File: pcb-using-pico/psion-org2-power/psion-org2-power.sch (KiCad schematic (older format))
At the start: 52 parts, among them J1 Conn_02x08_Odd_Even, J2 Conn_02x08_Odd_Even, J3 Conn_01x27_Female, J4 Conn_02x08_Odd_Even, J5 Conn_01x11_Female, J6 Conn_01x02_Female, J7 Conn_01x03_Female, M1 P-CHANNEL-MOSFET, M2 P-CHANNEL-MOSFET, U1 ESP32-WROOM-32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

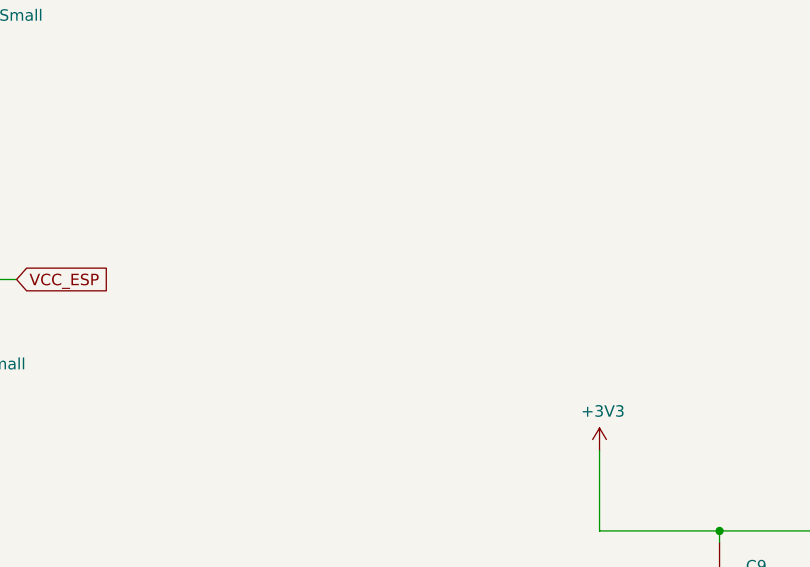
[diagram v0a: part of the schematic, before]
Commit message: V1.1 PCBs
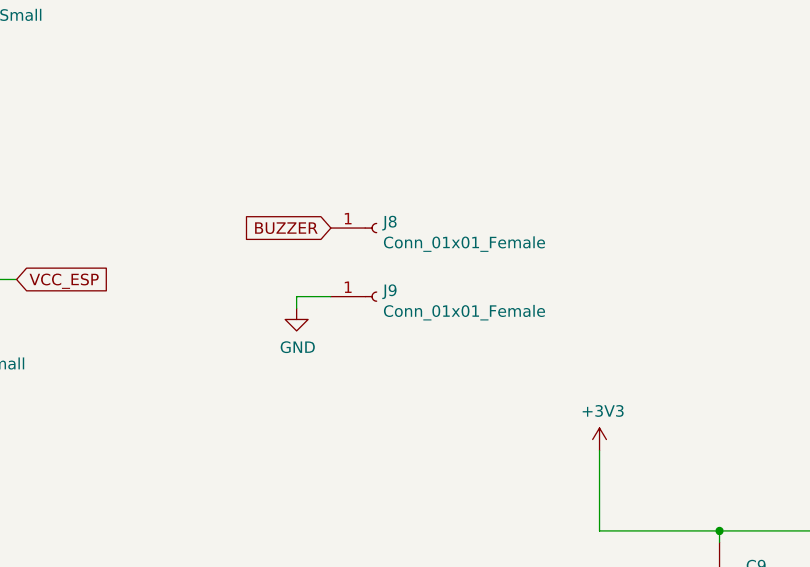
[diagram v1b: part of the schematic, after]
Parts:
- added J8, J9: Conn_01x01_Female, ajm_kicad:psion_beeper_pad, symbol Connector:Conn_01x01_Female
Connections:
- net BUZZER: now also J8.1 (Pin_1)
- net GND: now also J9.1 (Pin_1)
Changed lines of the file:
@@
 Wire Wire Line
 	14600 1800 14850 1800
+$Comp
+L Connector:Conn_01x01_Female J8
+U 1 1 622FDD65
+P 5600 6975
+F 0 "J8" H 5628 7001 50  0000 L CNN
+F 1 "Conn_01x01_Female" H 5628 6910 50  0000 L CNN
+F 2 "ajm_kicad:psion_beeper_pad" H 5600 6975 50  0001 C CNN
+F 3 "~" H 5600 6975 50  0001 C CNN
+	1    5600 6975
+	1    0    0    -1
+$EndComp
+$Comp
+L Connector:Conn_01x01_Female J9
+U 1 1 622FE035
+P 5600 7275
+F 0 "J9" H 5628 7301 50  0000 L CNN
+F 1 "Conn_01x01_Female" H 5628 7210 50  0000 L CNN
+F 2 "ajm_kicad:psion_beeper_pad" H 5600 7275 50  0001 C CNN
+F 3 "~" H 5600 7275 50  0001 C CNN
+	1    5600 7275
+	1    0    0    -1
+$EndComp
+$Comp
+L power:GND #PWR0132
+U 1 1 622FEC3B
+P 5250 7325
+F 0 "#PWR0132" H 5250 7075 50  0001 C CNN
+F 1 "GND" H 5255 7152 50  0000 C CNN
+F 2 "" H 5250 7325 50  0001 C CNN
+F 3 "" H 5250 7325 50  0001 C CNN
+	1    5250 7325
+	1    0    0    -1
+$EndComp
+Wire Wire Line
+	5250 7325 5250 7275
+Wire Wire Line
+	5250 7275 5400 7275
+Text GLabel 5400 6975 0    50   Input ~ 0
+BUZZER
 $EndSCHEMATC

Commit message: Updates
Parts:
- R1, R13, R14: value 100k -> 10k
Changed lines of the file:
@@
 P 2275 3125
 F 0 "R1" H 2334 3171 50  0000 L CNN
-F 1 "100k" H 2334 3080 50  0000 L CNN
+F 1 "10k" H 2334 3080 50  0000 L CNN
 F 2 "Resistor_SMD:R_0805_2012Metric" H 2275 3125 50  0001 C CNN
 F 3 "~" H 2275 3125 50  0001 C CNN
@@
 P 10075 6775
 F 0 "R13" H 10134 6821 50  0000 L CNN
-F 1 "100k" H 10134 6730 50  0000 L CNN
+F 1 "10k" H 10134 6730 50  0000 L CNN
 F 2 "Resistor_SMD:R_0805_2012Metric" H 10075 6775 50  0001 C CNN
 F 3 "~" H 10075 6775 50  0001 C CNN
@@
 P 10075 7500
 F 0 "R14" H 10134 7546 50  0000 L CNN
-F 1 "100k" H 10134 7455 50  0000 L CNN
+F 1 "10k" H 10134 7455 50  0000 L CNN
 F 2 "Resistor_SMD:R_0805_2012Metric" H 10075 7500 50  0001 C CNN
 F 3 "~" H 10075 7500 50  0001 C CNN

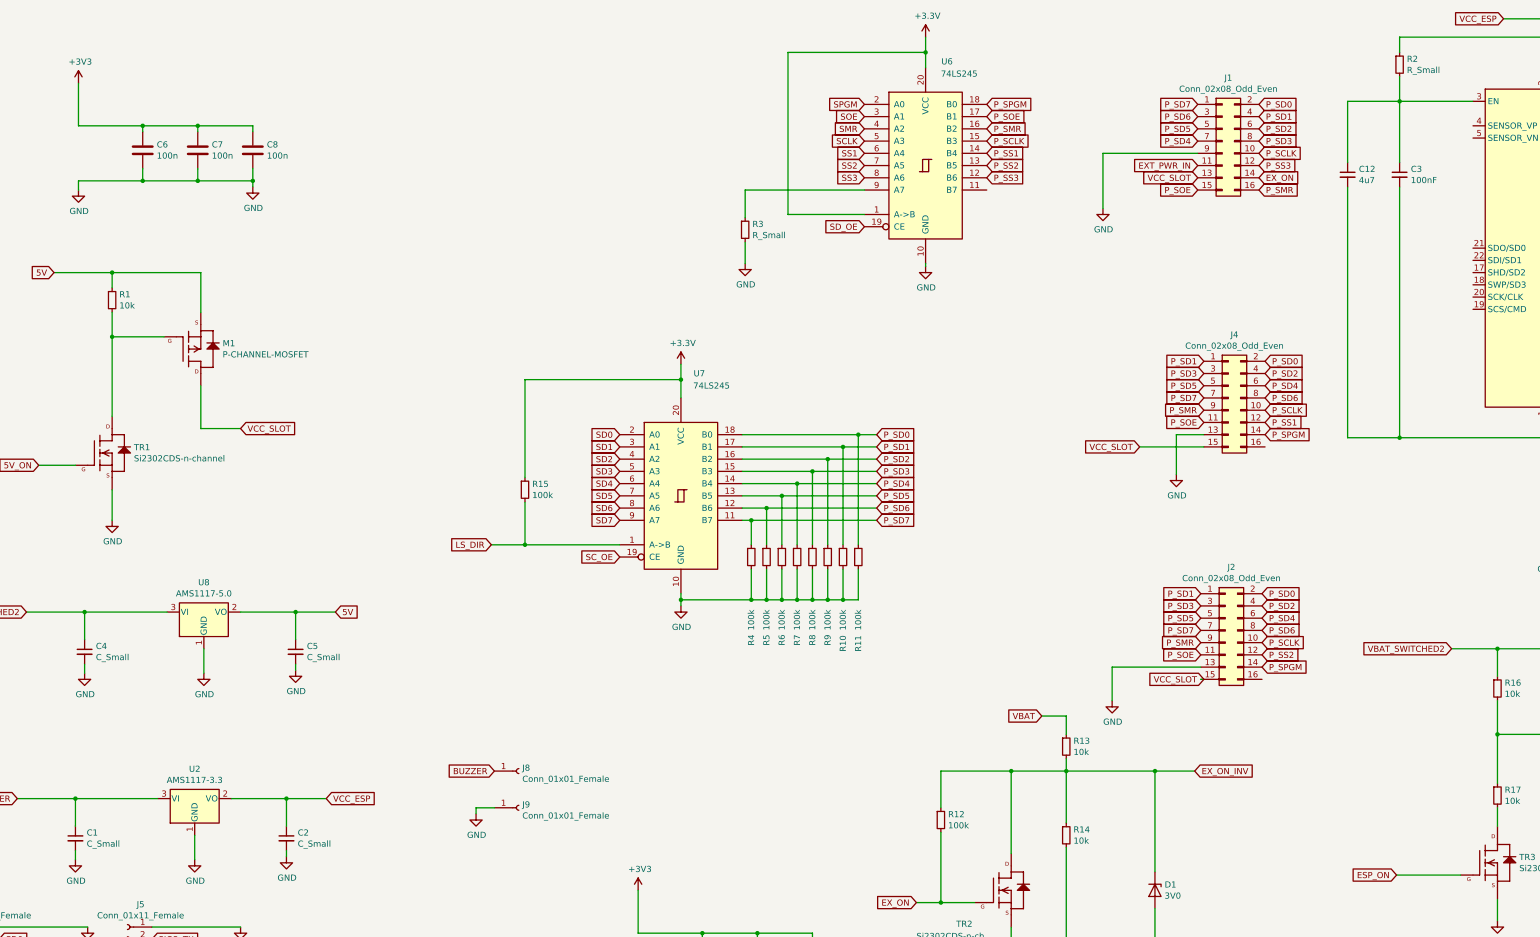
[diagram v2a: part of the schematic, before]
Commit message: Updated missing values on schematics, pushed those through to the PCB and created BOM .csv files for those schematics. Created .pdf files for schematics to mitigate the missing library problem of Kicad 5.
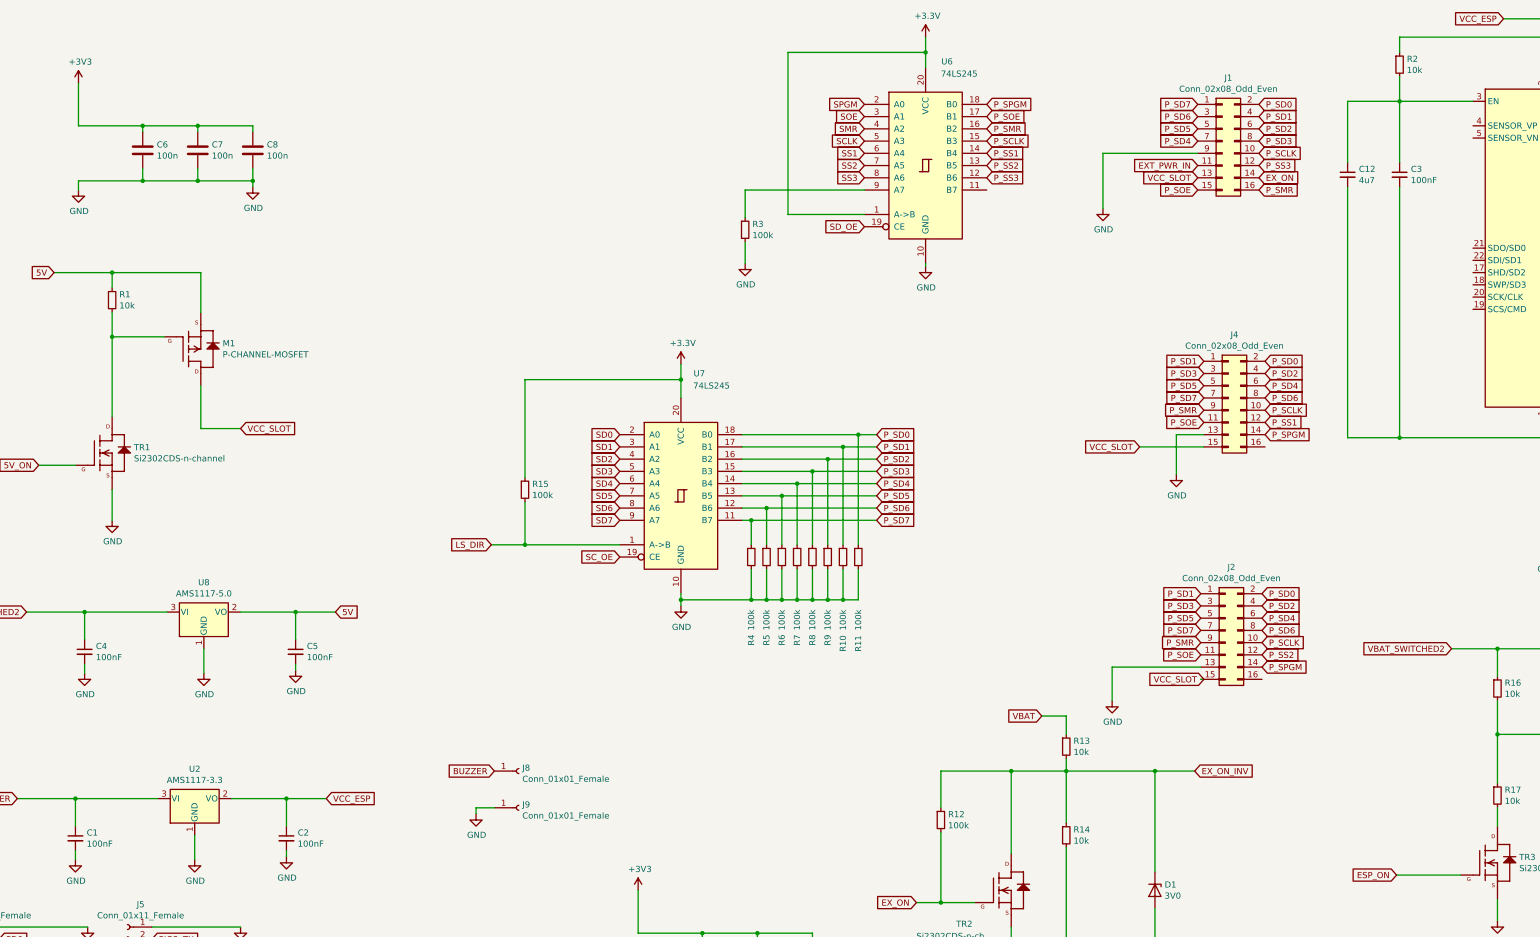
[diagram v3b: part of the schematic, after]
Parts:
- C1, C2, C4, C5: value C_Small -> 100nF
- R2: value R_Small -> 10k
- R3: value R_Small -> 100k
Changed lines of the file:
@@
 P 12800 1200
 F 0 "R2" H 12859 1246 50  0000 L CNN
-F 1 "R_Small" H 12859 1155 50  0000 L CNN
+F 1 "10k" H 12859 1155 50  0000 L CNN
 F 2 "Resistor_SMD:R_0805_2012Metric" H 12800 1200 50  0001 C CNN
 F 3 "~" H 12800 1200 50  0001 C CNN
@@
 P 1975 7525
 F 0 "C1" H 2067 7571 50  0000 L CNN
-F 1 "C_Small" H 2067 7480 50  0000 L CNN
+F 1 "100nF" H 2067 7480 50  0000 L CNN
 F 2 "Capacitor_SMD:C_0805_2012Metric" H 1975 7525 50  0001 C CNN
 F 3 "~" H 1975 7525 50  0001 C CNN
@@
 P 3700 7525
 F 0 "C2" H 3792 7571 50  0000 L CNN
-F 1 "C_Small" H 3792 7480 50  0000 L CNN
+F 1 "100nF" H 3792 7480 50  0000 L CNN
 F 2 "Capacitor_SMD:C_0805_2012Metric" H 3700 7525 50  0001 C CNN
 F 3 "~" H 3700 7525 50  0001 C CNN
@@
 P 2050 6000
 F 0 "C4" H 2142 6046 50  0000 L CNN
-F 1 "C_Small" H 2142 5955 50  0000 L CNN
+F 1 "100nF" H 2142 5955 50  0000 L CNN
 F 2 "Capacitor_SMD:C_0805_2012Metric" H 2050 6000 50  0001 C CNN
 F 3 "~" H 2050 6000 50  0001 C CNN
@@
 P 3775 6000
 F 0 "C5" H 3867 6046 50  0000 L CNN
-F 1 "C_Small" H 3867 5955 50  0000 L CNN
+F 1 "100nF" H 3867 5955 50  0000 L CNN
 F 2 "Capacitor_SMD:C_0805_2012Metric" H 3775 6000 50  0001 C CNN
 F 3 "~" H 3775 6000 50  0001 C CNN
@@
 P 7450 2550
 F 0 "R3" H 7509 2596 50  0000 L CNN
-F 1 "R_Small" H 7509 2505 50  0000 L CNN
+F 1 "100k" H 7509 2505 50  0000 L CNN
 F 2 "Resistor_SMD:R_0805_2012Metric" H 7450 2550 50  0001 C CNN
 F 3 "~" H 7450 2550 50  0001 C CNN
